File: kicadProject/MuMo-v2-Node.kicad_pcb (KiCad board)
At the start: 2 copper layers, 52.1 x 50 mm, 76 parts, among them Q1 Si1308EDL, SW1 Boot0, SW2 Reset, U1 MCP73123, U2 LoRa-E5, U3 CP2102N, U4 eInk_Display_1.54"200x200px, U5 BME680, U6 TSL25911, U7 BR24G512FVT-5AE2

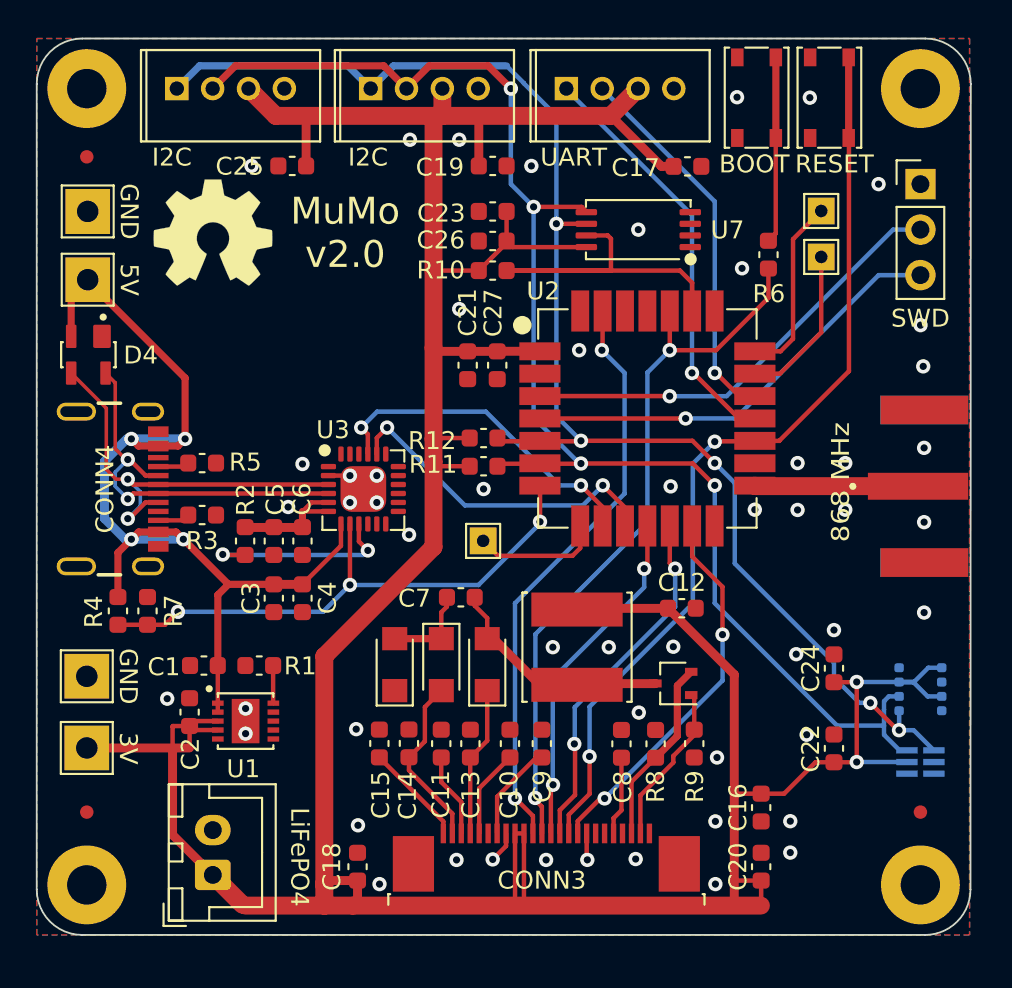
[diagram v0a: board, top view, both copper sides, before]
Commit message: V2.1
Minor update, fixing issues #2 #3 #6 #7 #8 #9 #10 #11 #12 #13 #14 #15 #16 #17 #18 and #19
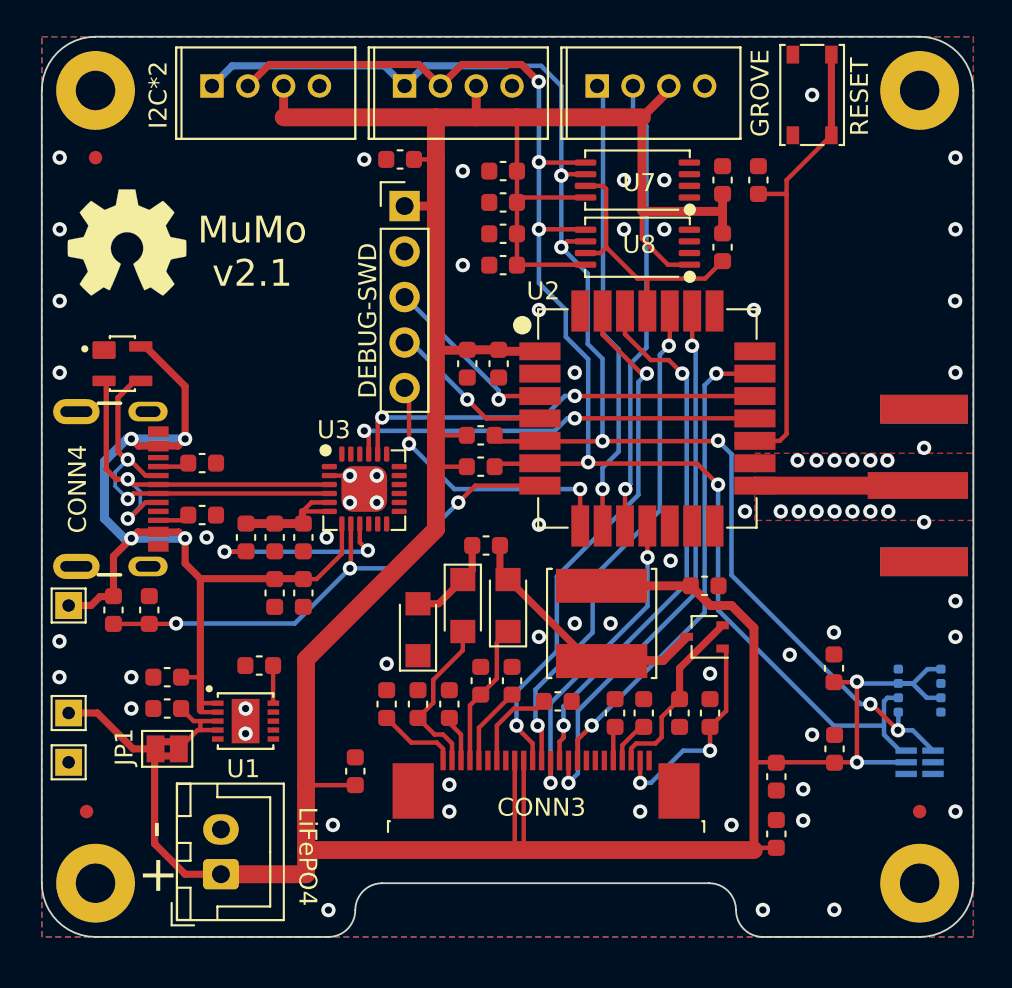
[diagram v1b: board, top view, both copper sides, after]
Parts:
- removed R6: 470, thisProjectLibrary:0603_1608Metric
- removed SW1: Boot0, thisProjectLibrary:SW_SPST_PTS815
- removed TP1, TP2, TP3: GND, TestPoint:TestPoint_THTPad_1.5x1.5mm_Drill0.7mm
- removed TP5: GND, TestPoint:TestPoint_THTPad_2.5x2.5mm_Drill1.2mm
- added C28: 4u7, thisProjectLibrary:0603_1608Metric, F.Cu at (181.0, 65.6)
- added C29: 100n, thisProjectLibrary:0603_1608Metric, F.Cu at (183.0, 65.6)
- added C30: 1uF/50V, thisProjectLibrary:0603_1608Metric, F.Cu at (176.6, 95.3)
- added JP1: Cut to disable charging, Jumper:SolderJumper-2_P1.3mm_Bridged2Bar_Pad1.0x1.5mm, F.Cu at (150.0, 97.3)
- added U8: BR24G512FVT-5AE2, thisProjectLibrary:TSSOP-B8, F.Cu at (176.3, 69.3)
- C15: value 1uF/50V -> 1uF/25V
- C17: value 4u7 -> 100n
- C23, C25: value 100n -> 4u7
- CONN1: value SWD -> DEBUG-SWD; footprint Connector_PinHeader_2.54mm:PinHeader_1x03_P2.54mm_Vertical -> Connector_PinHeader_2.54mm:PinHeader_1x05_P2.54mm_Vertical
- CONN6: value UART -> UART1
- D3: value SL03-GS08 -> SS1FL3HM3/H
- Q1: value Si1308EDL -> PJC7400
- R10, R11, R12: value 3K3 -> 5K1
- TP4, TP6: footprint TestPoint:TestPoint_THTPad_2.5x2.5mm_Drill1.2mm -> TestPoint:TestPoint_THTPad_1.5x1.5mm_Drill0.7mm
- TP7: value TestPoint_Probe -> 5V; footprint TestPoint:TestPoint_THTPad_2.5x2.5mm_Drill1.2mm -> TestPoint:TestPoint_THTPad_1.5x1.5mm_Drill0.7mm
- moved CONN1 28.8 mm to (163.3, 67.0)
- moved TP7 18.2 mm to (144.5, 89.3)
- moved R10 12.9 mm to (181.0, 69.3), turned to -90 degrees
- moved C17 10.5 mm to (168.8, 66.8), turned to 180 degrees
- moved C25 6.03 mm to (163.0, 64.4)
- moved C18 5.33 mm to (160.5, 98.6)
- moved TP4 4.91 mm to (144.5, 98.1)
- moved U4 4.83 mm to (147.8, 69.1)
- moved CONN3 4.07 mm to (171.2, 99.3)
- moved C13 3.55 mm to (167.5, 93.5)
- moved D2 3.51 mm to (166.5, 89.3)
- moved C10 3.51 mm to (169.3, 93.5)
- moved D3 3.50 mm to (169.1, 89.3)
- moved C7 3.22 mm to (167.8, 86.0)
- moved Q1 3.13 mm to (180.0, 91.1)
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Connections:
- net Net-(C10-Pad2) renamed VSH
- net Net-(C11-Pad2) renamed VSL
- net Net-(C13-Pad2) renamed PREVGH
- net Net-(C14-Pad2) renamed PREVGL
- net Net-(C15-Pad2) renamed VCOM
- net Net-(C8-Pad2) renamed VGH
- net Net-(CONN3-Pad2) renamed GATE-DRIVE
- net Net-(CONN3-Pad3) renamed CURRENT-SENSE
- net SCK renamed SPI2-SCK
- net SCL renamed I2C2-SCL
- net SDA renamed I2C2-SDA
- net SDI renamed SPI2-MOSI
- net /CS renamed DISPLAY-CS
- C12 pad 1: +3V3 -> +BATT
- C16 pad 1: +3V3 -> +BATT
- C17 pad 1: +3V3 -> +BATT
- C18 pad 1: +3V3 -> +BATT
- C19 pad 1: +3V3 -> +BATT
- C2 pad 1: +3V3 -> Net-(C2-Pad1)
- C20 pad 1: +3V3 -> +BATT
- C21 pad 1: +3V3 -> +BATT
- C22 pad 1: +3V3 -> +BATT
- C23 pad 1: +3V3 -> +BATT
- C24 pad 1: +3V3 -> +BATT
- C25 pad 1: +3V3 -> +BATT
- C26 pad 1: +3V3 -> +BATT
- C27 pad 1: +3V3 -> +BATT
- CONN1 pad 1: GND -> +BATT
- CONN1 pad 2: SWDIO -> GND
- CONN1 pad 3: SWCLK -> SWDIO
- CONN2 pad 1: +3V3 -> +BATT
- CONN3 pad 10: \RESET -> DISPLAY-RESET
- CONN3 pad 11: D/C -> DISPLAY-D/C
- CONN3 pad 15: +3V3 -> +BATT
- CONN3 pad 16: +3V3 -> +BATT
- CONN3 pad 4: unconnected-(CONN3-Pad4) -> VGL
- CONN3 pad 9: BUSY -> DISPLAY-BUSY
- CONN6 pad 1: USART_RX -> UART1-RX
- CONN6 pad 2: USART_TX -> UART1-TX
- CONN6 pad 3: +3V3 -> +BATT
- CONN7 pad 3: +3V3 -> +BATT
- CONN8 pad 3: +3V3 -> +BATT
- D4 pad 2: +5V -> D+
- D4 pad 3: D+ -> D-
- D4 pad 4: D- -> +5V
- L1 pad 2: +3V3 -> +BATT
- R10 pad 1: +3V3 -> +BATT
- R10 pad 2: WP -> WRITE-PROTECT
- R11 pad 1: +3V3 -> +BATT
- R12 pad 1: +3V3 -> +BATT
- SW2 pad 2: \RESET -> MCU-RESET
- TP6 pad 1: +3V3 -> +BATT
- U1 pad 3: +3V3 -> Net-(C2-Pad1)
- U1 pad 4: +3V3 -> Net-(C2-Pad1)
- U2 pad 1: +3V3 -> +BATT
- U2 pad 10: Net-(U2-Pad10) -> UART1-TX
- U2 pad 12: D/C -> unconnected-(U2-Pad12)
- U2 pad 13: BUSY -> unconnected-(U2-Pad13)
- U2 pad 17: \RESET -> MCU-RESET
- U2 pad 18: USART_RX -> UART2-RX
- U2 pad 19: USART_TX -> UART2-TX
- U2 pad 20: Net-(TP3-Pad1) -> DISPLAY-BUSY
- U2 pad 21: Net-(TP2-Pad1) -> unconnected-(U2-Pad21)
- U2 pad 23: WP -> DISPLAY-RESET
- U2 pad 25: unconnected-(U2-Pad25) -> WRITE-PROTECT
- U2 pad 26: unconnected-(U2-Pad26) -> DISPLAY-D/C
- U2 pad 8: Net-(TP1-Pad1) -> SWO
- U2 pad 9: Net-(U2-Pad9) -> UART1-RX
- U3 pad 20: Net-(U2-Pad10) -> UART2-TX
- U3 pad 21: Net-(U2-Pad9) -> UART2-RX
- U5 pad 2: +3V3 -> +BATT
- U5 pad 6: +3V3 -> +BATT
- U5 pad 8: +3V3 -> +BATT
- U6 pad 5: +3V3 -> +BATT
- U7 pad 7: WP -> WRITE-PROTECT
- U7 pad 8: +3V3 -> +BATT
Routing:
- net +3V3: track 229.6 -> 0.00 mm, vias 2 -> 0
- net +BATT: track 0.00 -> 219.5 mm, vias 0 -> 2
- net \RESET: track 51.9 -> 0.00 mm, vias 2 -> 0
- net DISPLAY-RESET: track 0.00 -> 30.6 mm, vias 0 -> 2
- net DISPLAY-D/C: track 0.00 -> 30.0 mm, vias 0 -> 2
- net DISPLAY-BUSY: track 0.00 -> 27.0 mm, vias 0 -> 2
- net MCU-RESET: track 0.00 -> 25.7 mm
- net UART1-RX: track 0.00 -> 25.4 mm, vias 0 -> 1
- net UART1-TX: track 0.00 -> 25.4 mm, vias 0 -> 1
- net UART2-RX: track 0.00 -> 23.5 mm, vias 0 -> 2
- net UART2-TX: track 0.00 -> 23.5 mm, vias 0 -> 2
- net USART_RX: track 23.3 -> 0.00 mm, vias 1 -> 0
- net BUSY: track 21.4 -> 0.00 mm, vias 2 -> 0
- net USART_TX: track 21.3 -> 0.00 mm, vias 1 -> 0
- net WP: track 21.2 -> 0.00 mm
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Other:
- board size 52.1 x 50 mm -> 52 x 50.3 mm
- board text added: "+"
- board text added: "-"
- board text added: "MuMo v2.1"
- board text added: "https://github.com/Strooom/MuMo-V2-Node-PCB"
- board text removed: "MuMo v2.0"

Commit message: cleanup references
sequential numbering for all identical parts
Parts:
- C11: renamed from C30; value 1uF/50V -> 1uF
- C12: renamed from C8; value 1uF/50V -> 1uF
- C13: renamed from C9; value 1uF/50V -> 1uF
- C14: renamed from C10; value 1uF/50V -> 1uF
- C15: renamed from C11; value 1uF/50V -> 1uF
- C16: renamed from C15; value 1uF/25V -> 1uF
- C17: renamed from C14; value 1uF/50V -> 1uF
- C18: renamed from C13; value 1uF/50V -> 1uF
- CONN6: value UART1 -> Grove Vertical THT
- CONN7, CONN8: value I2C -> Grove Vertical THT
- D1, D2: value SL03-GS08 -> SS1FL3HM3/H
- TP1: renamed from TP4; value GND -> testPad
- TP2: renamed from TP6; value 3V3 -> testPad
- TP3: renamed from TP7; value 5V -> testPad
- renumbered C24 to C1, C26 to C2, C16 to C21, C28 to C22, C18 to C23, C19 to C24, C20 to C25, C21 to C26, C23 to C27, C25 to C28, C3 to C29, C27 to C3, C5 to C30, C7 to C31, C1 to C32, C17 to C4, C12 to C41, C2 to C42, C22 to C5, C4 to C6, C6 to C7, C29 to C8, R8 to R1, R11 to R10, R12 to R11, R1 to R2, R2 to R3, R9 to R4, R4 to R5, R7 to R6, R3 to R7, R5 to R8, R10 to R9, SW2 to SW1

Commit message: added logo
Flanders
State of the Art
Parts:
- added G***: LOGO, thisProjectLibrary:logoFlanders, B.Cu at (171.0, 91.3)

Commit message: Improving the BOM
Grouped designators,
Added logo to silkscreen
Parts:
- added G***: LOGO, thisProjectLibrary:cc-logo, F.Cu at (152.5, 68.1)
- L1: value 68uH -> 47uH
- R1: value 0R47 -> 2R2
- moved U4 9.10 mm to (155.0, 74.6)

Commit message: updated gerbers for Seeed Studio Manufacturing
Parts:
- CONN6, CONN7, CONN8: value Grove Vertical THT -> Grove Vertical

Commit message: corrected battery connector
To align with most common premade cables, pin 1 = GND, pin 2 - VBAT
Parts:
- CONN6, CONN7, CONN8: value Grove Vertical -> Grove Vertical THT
- moved CONN2 2.51 mm to (152.8, 101.8), turned to -90 degrees
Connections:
- CONN2 pad 1: +BATT -> GND
- CONN2 pad 2: GND -> +BATT
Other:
- board text added: "MuMo v2.2"
- board text removed: "MuMo v2.1"
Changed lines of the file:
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@@
       (effects (font (size 1 1) (thickness 0.15)))
     )
-    (fp_text value "Grove Vertical" (at 0 1.75) (layer "F.Fab")
+    (fp_text value "Grove Vertical THT" (at 0 1.75) (layer "F.Fab")
       (effects (font (size 0.8 0.8) (thickness 0.1)))
     )
@@
     (property "unitPrice" "1.52")
     (attr through_hole)
-    (fp_text reference "U1" (at -0.127 2.667) (layer "F.SilkS")
+    (fp_text reference "U1" (at 2.9242 -0.05 90) (layer "F.SilkS")
       (effects (font (size 1.00163 1.00163) (thickness 0.15)))
     )
@@
   )
   (footprint "Connector_JST:JST_XH_B2B-XH-A_1x02_P2.50mm_Vertical" (layer "F.Cu")
-    (at 153.0308 104.308 90)
+    (at 152.8308 101.808 -90)
     (descr "JST XH series connector, B2B-XH-A (http://www.jst-mfg.com/product/pdf/eng/eXH.pdf), generated with kicad-footprint-generator")
     (tags "connector JST XH vertical")
@@
       (effects (font (size 1 1) (thickness 0.15)))
     )
-    (fp_text value "B2B-XH-A (LF)(SN)" (at -3.75 4.75 180) (layer "F.Fab") hide
+    (fp_text value "B2B-XH-A (LF)(SN)" (at -3.75 4.75) (layer "F.Fab") hide
       (effects (font (size 1 1) (thickness 0.15)))
     )
-    (fp_text user "LiFePO4" (at 0.996 4.843 270 unlocked) (layer "F.SilkS")
+    (fp_text user "LiFePO4" (at 1.1 -4.9 90 unlocked) (layer "F.SilkS")
       (effects (font (size 1 1) (thickness 0.15)))
     )
@@
     (fp_line (start 4.95 -2.35) (end -2.45 -2.35) (layer "F.Fab") (width 0.1))
     (fp_line (start -2.45 3.4) (end 4.95 3.4) (layer "F.Fab") (width 0.1))
-    (pad "1" thru_hole roundrect (at 0 0 90) (size 1.7 2) (drill 1) (layers *.Cu *.Mask) (roundrect_rratio 0.1470588235)
-      (net 61 "+BATT") (pinfunction "BAT+") (pintype "passive"))
-    (pad "2" thru_hole oval (at 2.5 0 90) (size 1.7 2) (drill 1) (layers *.Cu *.Mask)
-      (net 1 "GND") (pinfunction "BAT-") (pintype "passive"))
+    (pad "1" thru_hole roundrect (at 0 0 270) (size 1.7 2) (drill 1) (layers *.Cu *.Mask) (roundrect_rratio 0.1470588235)
+      (net 1 "GND") (pinfunction "BAT+") (pintype "passive"))
+    (pad "2" thru_hole oval (at 2.5 0 270) (size 1.7 2) (drill 1) (layers *.Cu *.Mask)
+      (net 61 "+BATT") (pinfunction "BAT-") (pintype "passive"))
     (model "${KICAD6_3DMODEL_DIR}/Connector_JST.3dshapes/JST_XH_B2B-XH-A_1x02_P2.50mm_Vertical.wrl"
       (offset (xyz 0 0 0))
@@
       (effects (font (size 1 1) (thickness 0.15)))
     )
-    (fp_text value "Grove Vertical" (at 0 1.75) (layer "F.Fab")
+    (fp_text value "Grove Vertical THT" (at 0 1.75) (layer "F.Fab")
       (effects (font (size 0.8 0.8) (thickness 0.1)))
     )
@@
       (effects (font (size 1 1) (thickness 0.15)))
     )
-    (fp_text value "Grove Vertical" (at 0 1.75) (layer "F.Fab")
+    (fp_text value "Grove Vertical THT" (at 0 1.75) (layer "F.Fab")
       (effects (font (size 0.8 0.8) (thickness 0.1)))
     )
@@
     (effects (font (size 1 1) (thickness 0.15)) (justify mirror))
   )
-  (gr_text "MuMo v2.1" (at 191.5308 69.808 270) (layer "F.SilkS")
+  (gr_text "MuMo v2.2" (at 191.5308 69.808 270) (layer "F.SilkS")
     (effects (font (size 1.5 1.5) (thickness 0.25)))
   )
-  (gr_text "-" (at 149.2808 101.808 90) (layer "F.SilkS")
-    (effects (font (size 2 2) (thickness 0.15)))
+  (gr_text "-" (at 156.4308 99.908 90) (layer "F.SilkS")
+    (effects (font (size 2.5 2.5) (thickness 0.2)))
   )
-  (gr_text "+" (at 149.5308 104.308) (layer "F.SilkS")
-    (effects (font (size 2 2) (thickness 0.15)))
+  (gr_text "+" (at 156.6308 106.008) (layer "F.SilkS")
+    (effects (font (size 2.5 2.5) (thickness 0.2)))
   )
   (segment (start 159.0808 82.054) (end 160.2308 82.054) (width 0.25) (layer "F.Cu") (net 1))
@@
   (segment (start 182.7808 90.558) (end 181.5308 89.308) (width 0.5) (layer "F.Cu") (net 61))
   (segment (start 169.9308 102.958) (end 169.9308 97.958) (width 0.25) (layer "F.Cu") (net 61))
+  (segment (start 151.0308 104.308) (end 152.8308 104.308) (width 0.4) (layer "F.Cu") (net 61))
   (segment (start 169.5558 62.083) (end 169.5308 62.058) (width 0.25) (layer "F.Cu") (net 61))
   (segment (start 169.8308 66.533) (end 169.5558 66.808) (width 0.25) (layer "F.Cu") (net 61))
   (segment (start 187.2558 98.058) (end 184.0558 98.058) (width 0.25) (layer "F.Cu") (net 61))
-  (segment (start 157.7808 104.308) (end 153.0308 104.308) (width 1) (layer "F.Cu") (net 61))
   (segment (start 166.7558 79.808) (end 165.0308 79.808) (width 0.25) (layer "F.Cu") (net 61))
   (segment (start 165.0308 64.408) (end 165.0308 85.058) (width 1) (layer "F.Cu") (net 61))
@@
   (segment (start 174.2808 88.208) (end 179.2558 88.208) (width 0.5) (layer "F.Cu") (net 61))
   (segment (start 166.7808 75.033) (end 166.7558 75.058) (width 0.5) (layer "F.Cu") (net 61))
+  (segment (start 149.3808 97.308) (end 149.3308 97.358) (width 0.4) (layer "F.Cu") (net 61))
   (segment (start 182.7808 102.958) (end 182.7808 90.558) (width 0.5) (layer "F.Cu") (net 61))
-  (segment (start 151.0308 104.308) (end 153.0308 104.308) (width 0.4) (layer "F.Cu") (net 61))
   (segment (start 144.5308 95.308) (end 146.1308 95.308) (width 0.4) (layer "F.Cu") (net 61))
   (segment (start 157.8058 99.333) (end 157.7808 99.308) (width 0.25) (layer "F.Cu") (net 61))
@@
   (segment (start 148.1308 97.308) (end 149.3808 97.308) (width 0.4) (layer "F.Cu") (net 61))
   (segment (start 169.4308 97.958) (end 169.4308 102.908) (width 0.25) (layer "F.Cu") (net 61))
+  (segment (start 149.3308 102.608) (end 151.0308 104.308) (width 0.4) (layer "F.Cu") (net 61))
   (segment (start 169.5558 70.308) (end 169.5558 62.083) (width 0.25) (layer "F.Cu") (net 61))
   (segment (start 168.5308 75.033) (end 166.7808 75.033) (width 0.5) (layer "F.Cu") (net 61))
@@
   (segment (start 181.5308 89.308) (end 180.3558 89.308) (width 0.5) (layer "F.Cu") (net 61))
   (segment (start 169.4308 102.908) (end 169.3808 102.958) (width 0.25) (layer "F.Cu") (net 61))
-  (segment (start 149.3308 102.608) (end 151.0308 104.308) (width 0.4) (layer "F.Cu") (net 61))
   (segment (start 181.0308 66.333) (end 181.0308 68.533) (width 0.5) (layer "F.Cu") (net 61))
   (segment (start 176.5308 62.058) (end 176.5308 67.308) (width 0.5) (layer "F.Cu") (net 61))
@@
   (segment (start 167.2808 62.058) (end 169.5308 62.058) (width 1) (layer "F.Cu") (net 61))
   (segment (start 157.7808 92.308) (end 157.7808 99.308) (width 1) (layer "F.Cu") (net 61))
+  (segment (start 149.3308 97.358) (end 149.3308 102.608) (width 0.4) (layer "F.Cu") (net 61))
   (segment (start 173.3808 66.533) (end 169.8308 66.533) (width 0.25) (layer "F.Cu") (net 61))
   (segment (start 180.3558 89.308) (end 179.2558 88.208) (width 0.5) (layer "F.Cu") (net 61))
@@
   (segment (start 184.0058 98.058) (end 182.7808 98.058) (width 0.25) (layer "F.Cu") (net 61))
   (segment (start 168.5308 75.0422) (end 168.5308 75.033) (width 0.25) (layer "F.Cu") (net 61))
-  (segment (start 149.3308 97.358) (end 149.3308 102.608) (width 0.4) (layer "F.Cu") (net 61))
+  (segment (start 157.7808 104.308) (end 152.8308 104.308) (width 1) (layer "F.Cu") (net 61))
   (segment (start 182.7808 102.958) (end 182.9058 102.833) (width 0.25) (layer "F.Cu") (net 61))
   (segment (start 188.5308 98.058) (end 187.3058 98.058) (width 0.25) (layer "F.Cu") (net 61))
-  (segment (start 149.3808 97.308) (end 149.3308 97.358) (width 0.4) (layer "F.Cu") (net 61))
   (segment (start 184.0308 98.083) (end 184.0058 98.058) (width 0.25) (layer "F.Cu") (net 61))
   (segment (start 166.7558 75.058) (end 165.087 75.058) (width 0.5) (layer "F.Cu") (net 61))
   (segment (start 168.456 75.117) (end 168.5308 75.0422) (width 0.25) (layer "F.Cu") (net 61))
+  (segment (start 157.7808 99.308) (end 157.7808 104.308) (width 1) (layer "F.Cu") (net 61))
   (segment (start 188.5022 93.5866) (end 187.2488 93.5866) (width 0.25) (layer "F.Cu") (net 61))
   (segment (start 157.7808 102.958) (end 182.7808 102.958) (width 1) (layer "F.Cu") (net 61))
-  (segment (start 157.7808 99.308) (end 157.7808 104.308) (width 1) (layer "F.Cu") (net 61))
   (segment (start 160.5308 99.333) (end 157.8058 99.333) (width 0.25) (layer "F.Cu") (net 61))
   (segment (start 165.0308 85.058) (end 157.7808 92.308) (width 1) (layer "F.Cu") (net 61))
@@
         (xy 195.0308 84.558)
         (xy 182.8308 84.558)
-        (xy 182.8308 80.808)
-        (xy 195.0308 80.808)
+        (xy 182.8308 80.708)
+        (xy 195.0308 80.708)
       )
     )
@@
         (xy 195.0308 84.558)
         (xy 183.0308 84.558)
-        (xy 183.0308 80.808)
-        (xy 195.0308 80.808)
+        (xy 183.0308 80.708)
+        (xy 195.0308 80.708)
       )
     )
